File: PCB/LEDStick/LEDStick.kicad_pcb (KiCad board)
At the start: 4 copper layers, 8.8 x 52.2 mm, 27 parts, among them J1 Conn_01x04_Pin

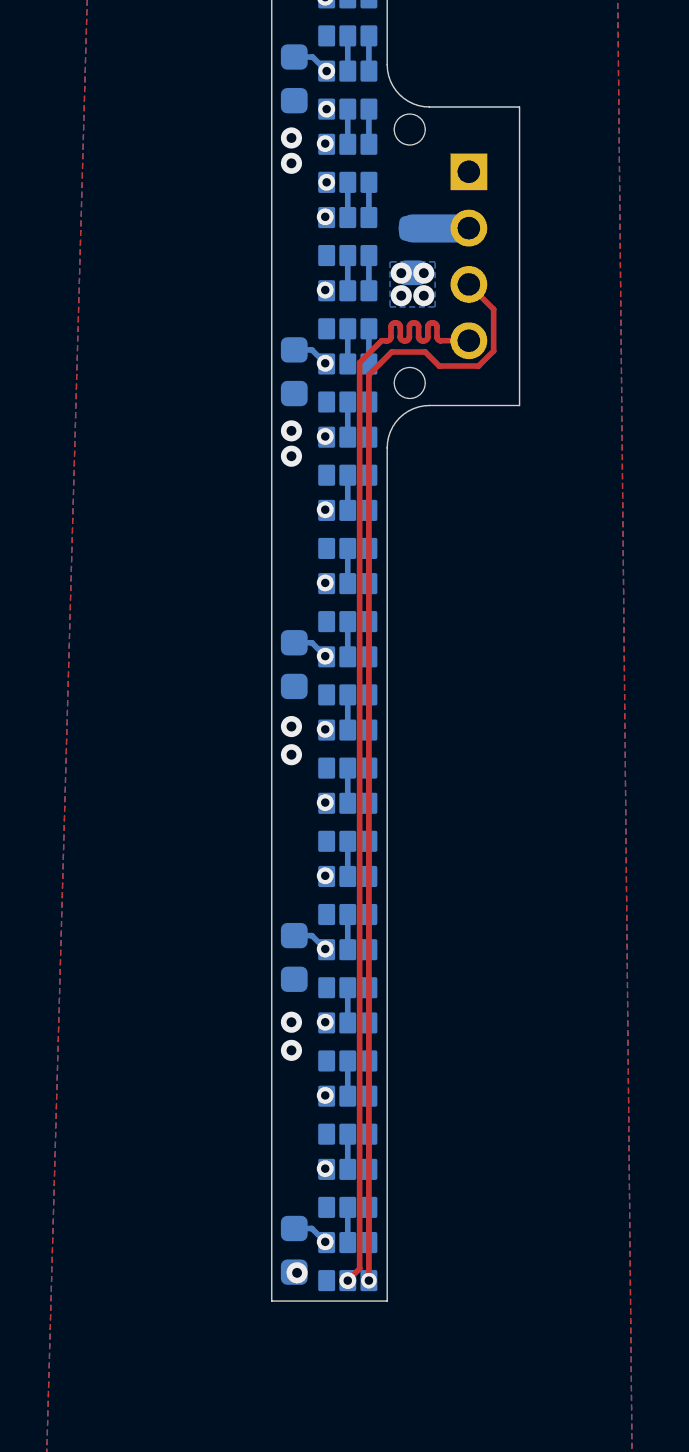
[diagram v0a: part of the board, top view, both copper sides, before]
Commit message: main layout complete needs headers and testpoints
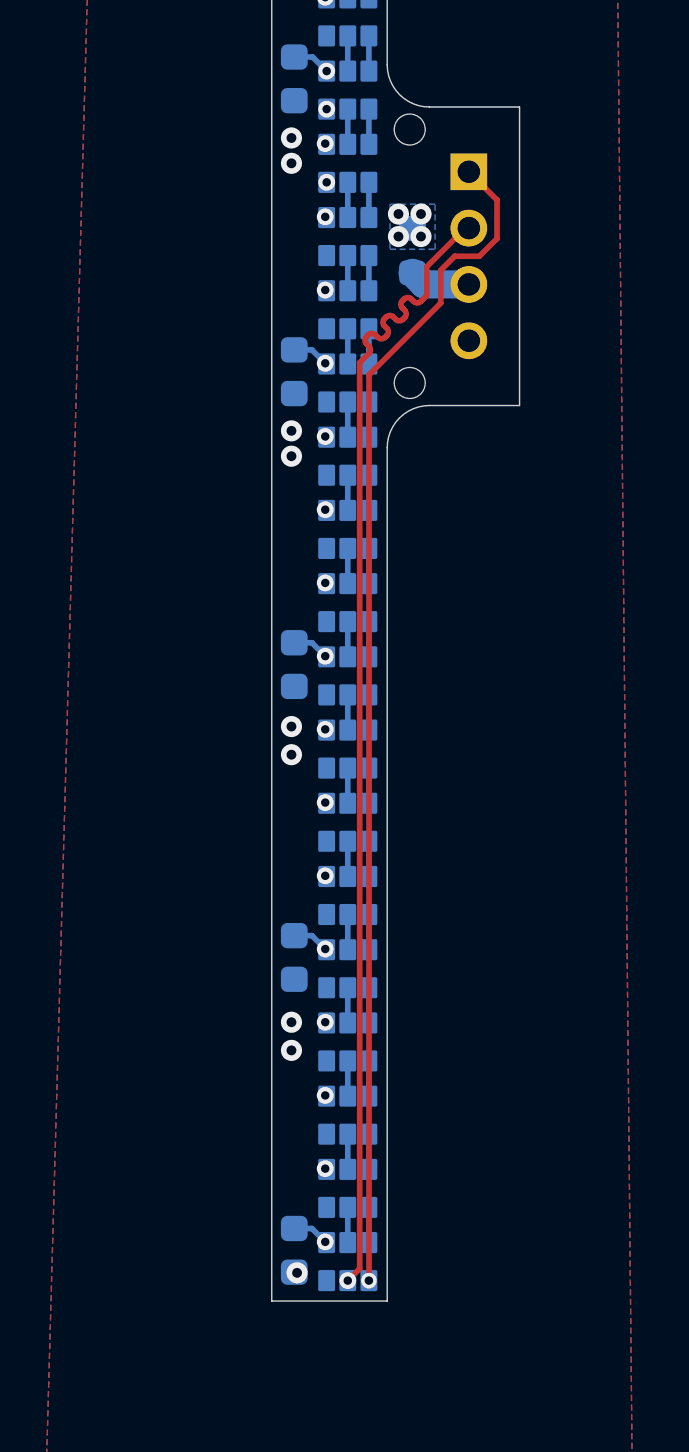
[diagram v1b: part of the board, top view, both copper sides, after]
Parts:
- turned F1 to -90 degrees
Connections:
- F1 pad 2: Net-(J1-Pin_2) -> Net-(J1-Pin_3)
- J1 pad 1: GND -> Net-(D1-DI)
- J1 pad 2: Net-(J1-Pin_2) -> Net-(D1-CI)
- J1 pad 3: Net-(D1-DI) -> Net-(J1-Pin_3)
- J1 pad 4: Net-(D1-CI) -> GND
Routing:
- net Net-(J1-Pin_3): track 0.00 -> 2.17 mm
- net Net-(D1-DI): track 40.1 -> 42.2 mm
- net Net-(J1-Pin_2): track 2.01 -> 0.00 mm
- net Net-(D1-CI): track 40.0 -> 41.1 mm

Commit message: boards ordered
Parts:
- moved D1 64.9 mm to (77.3, 33.8), turned to 0 degrees
- moved C1 64.6 mm to (76.9, 35.7), turned to 0 degrees
- moved D2 61.3 mm to (74.7, 33.8), turned to 0 degrees
- moved D3 57.6 mm to (72.1, 33.8), turned to 0 degrees
- moved D4 53.9 mm to (69.5, 33.8), turned to 0 degrees
- moved D5 50.3 mm to (66.9, 33.8), turned to 0 degrees
- moved C2 50.1 mm to (66.5, 35.7), turned to 0 degrees
- moved D6 46.6 mm to (64.3, 33.8), turned to 0 degrees
- moved D7 43.0 mm to (61.7, 33.8), turned to 0 degrees
- moved D8 39.3 mm to (59.1, 33.8), turned to 0 degrees
- moved D9 35.7 mm to (56.5, 33.8), turned to 0 degrees
- moved C3 35.6 mm to (56.1, 35.7), turned to 0 degrees
- moved D10 32.1 mm to (53.9, 33.8), turned to 0 degrees
- moved D11 28.4 mm to (51.3, 33.8), turned to 0 degrees
- moved D12 24.8 mm to (48.7, 33.8), turned to 0 degrees
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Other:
- board size 8.8 x 52.2 mm -> 52.2 x 8.8 mm
